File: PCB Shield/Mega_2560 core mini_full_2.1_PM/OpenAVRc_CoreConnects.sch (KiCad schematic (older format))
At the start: 18 parts, among them P1 2560-core, P10 RX1TX1, P16 LCD, P6 Micro_sd, P9 SPI, Q1 BSS84

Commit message: Update pcb files v2.1
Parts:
- added R10: 100, Resistors_SMD:R_1206, symbol R-RESCUE-Mega_2560_core_mini_full_2.0
- RV1: value 220K -> 10K
- RV6: value 22K -> 500
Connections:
- net at P16.18 (P18): now also R10.1; no longer RV6.2
- new net: R10.2, RV6.2
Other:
- moved on the sheet: RV6
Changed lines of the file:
@@
 Sheet 3 7
 Title "Shield Mega2560 core Full"
-Date "2018-01-30"
+Date "2018-01-31"
 Rev "2.10"
 Comp "© Team OpenAVRc"
@@
 $EndComp
 $Comp
-L GND-RESCUE-Mega_2560_core_mini_full_2.0 #PWR044
+L GND-RESCUE-Mega_2560_core_mini_full_2.0 #PWR51
 U 1 1 59C5DDBC
 P 4250 4450
-F 0 "#PWR044" H 4250 4200 50  0001 C CNN
+F 0 "#PWR51" H 4250 4200 50  0001 C CNN
 F 1 "GND" H 4250 4300 50  0000 C CNN
 F 2 "" H 4250 4450 50  0000 C CNN
@@
 $EndComp
 $Comp
-L VCC #PWR045
+L VCC #PWR49
 U 1 1 59C5DDC2
 P 3900 4700
-F 0 "#PWR045" H 3900 4550 50  0001 C CNN
+F 0 "#PWR49" H 3900 4550 50  0001 C CNN
 F 1 "VCC" V 3900 4900 50  0000 C CNN
 F 2 "" H 3900 4700 50  0000 C CNN
@@
 $EndComp
 $Comp
-L GND-RESCUE-Mega_2560_core_mini_full_2.0 #PWR046
+L GND-RESCUE-Mega_2560_core_mini_full_2.0 #PWR47
 U 1 1 59C5DDC8
 P 3400 1700
-F 0 "#PWR046" H 3400 1450 50  0001 C CNN
+F 0 "#PWR47" H 3400 1450 50  0001 C CNN
 F 1 "GND" H 3400 1550 50  0000 C CNN
 F 2 "" H 3400 1700 50  0000 C CNN
@@
 $EndComp
 $Comp
-L VCC #PWR047
+L VCC #PWR48
 U 1 1 59C5DDCE
 P 3700 1700
-F 0 "#PWR047" H 3700 1550 50  0001 C CNN
+F 0 "#PWR48" H 3700 1550 50  0001 C CNN
 F 1 "VCC" H 3700 1850 50  0000 C CNN
 F 2 "" H 3700 1700 50  0000 C CNN
@@
 Mosi
 $Comp
-L GND-RESCUE-Mega_2560_core_mini_full_2.0 #PWR048
+L GND-RESCUE-Mega_2560_core_mini_full_2.0 #PWR55
 U 1 1 59C5DDDC
 P 4900 2450
-F 0 "#PWR048" H 4900 2200 50  0001 C CNN
+F 0 "#PWR55" H 4900 2200 50  0001 C CNN
 F 1 "GND" V 4900 2250 50  0000 C CNN
 F 2 "" H 4900 2450 50  0000 C CNN
@@
 $EndComp
 $Comp
-L VCC #PWR049
+L VCC #PWR54
 U 1 1 59C5DDE2
 P 4900 2250
-F 0 "#PWR049" H 4900 2100 50  0001 C CNN
+F 0 "#PWR54" H 4900 2100 50  0001 C CNN
 F 1 "VCC" V 4900 2450 50  0000 C CNN
 F 2 "" H 4900 2250 50  0000 C CNN
@@
 $EndComp
 $Comp
-L VCC #PWR050
+L VCC #PWR46
 U 1 1 59C5DDE8
 P 2600 2100
-F 0 "#PWR050" H 2600 1950 50  0001 C CNN
+F 0 "#PWR46" H 2600 1950 50  0001 C CNN
 F 1 "VCC" V 2600 2300 50  0000 C CNN
 F 2 "" H 2600 2100 50  0000 C CNN
@@
 Lcd_bla
 $Comp
-L GND-RESCUE-Mega_2560_core_mini_full_2.0 #PWR051
+L GND-RESCUE-Mega_2560_core_mini_full_2.0 #PWR44
 U 1 1 59C5DE25
 P 1850 4450
-F 0 "#PWR051" H 1850 4200 50  0001 C CNN
+F 0 "#PWR44" H 1850 4200 50  0001 C CNN
 F 1 "GND" H 1850 4300 50  0000 C CNN
 F 2 "" H 1850 4450 50  0000 C CNN
@@
 $EndComp
 $Comp
-L GND-RESCUE-Mega_2560_core_mini_full_2.0 #PWR052
+L GND-RESCUE-Mega_2560_core_mini_full_2.0 #PWR45
 U 1 1 59C5DE2D
 P 2350 5300
-F 0 "#PWR052" H 2350 5050 50  0001 C CNN
+F 0 "#PWR45" H 2350 5050 50  0001 C CNN
 F 1 "GND" H 2350 5150 50  0000 C CNN
 F 2 "" H 2350 5300 50  0000 C CNN
@@
 $EndComp
 $Comp
-L GND-RESCUE-Mega_2560_core_mini_full_2.0 #PWR053
+L GND-RESCUE-Mega_2560_core_mini_full_2.0 #PWR52
 U 1 1 59C5DE45
 P 4550 4450
-F 0 "#PWR053" H 4550 4200 50  0001 C CNN
+F 0 "#PWR52" H 4550 4200 50  0001 C CNN
 F 1 "GND" H 4550 4300 50  0000 C CNN
 F 2 "" H 4550 4450 50  0000 C CNN
@@
 $EndComp
 $Comp
-L GND-RESCUE-Mega_2560_core_mini_full_2.0 #PWR054
+L GND-RESCUE-Mega_2560_core_mini_full_2.0 #PWR50
 U 1 1 59C5DE66
 P 4150 4950
-F 0 "#PWR054" H 4150 4700 50  0001 C CNN
+F 0 "#PWR50" H 4150 4700 50  0001 C CNN
 F 1 "GND" H 4150 4800 50  0000 C CNN
 F 2 "" H 4150 4950 50  0000 C CNN
@@
 $EndComp
 $Comp
-L GND-RESCUE-Mega_2560_core_mini_full_2.0 #PWR055
+L GND-RESCUE-Mega_2560_core_mini_full_2.0 #PWR43
 U 1 1 59C5DE7A
 P 1400 2100
-F 0 "#PWR055" H 1400 1850 50  0001 C CNN
+F 0 "#PWR43" H 1400 1850 50  0001 C CNN
 F 1 "GND" H 1400 1950 50  0000 C CNN
 F 2 "" H 1400 2100 50  0000 C CNN
@@
 $EndComp
 $Comp
-L GND-RESCUE-Mega_2560_core_mini_full_2.0 #PWR056
+L GND-RESCUE-Mega_2560_core_mini_full_2.0 #PWR53
 U 1 1 59C5DE80
 P 4850 2100
-F 0 "#PWR056" H 4850 1850 50  0001 C CNN
+F 0 "#PWR53" H 4850 1850 50  0001 C CNN
 F 1 "GND" V 4850 1900 50  0000 C CNN
 F 2 "" H 4850 2100 50  0000 C CNN
@@
 $EndComp
 $Comp
-L GND-RESCUE-Mega_2560_core_mini_full_2.0 #PWR057
+L GND-RESCUE-Mega_2560_core_mini_full_2.0 #PWR57
 U 1 1 59C5BE4B
 P 7050 2100
-F 0 "#PWR057" H 7050 1850 50  0001 C CNN
+F 0 "#PWR57" H 7050 1850 50  0001 C CNN
 F 1 "GND" H 7050 1950 50  0000 C CNN
 F 2 "" H 7050 2100 50  0000 C CNN
@@
 $EndComp
 $Comp
-L VCC #PWR058
+L VCC #PWR56
 U 1 1 59C5BE51
 P 6750 2100
-F 0 "#PWR058" H 6750 1950 50  0001 C CNN
+F 0 "#PWR56" H 6750 1950 50  0001 C CNN
 F 1 "VCC" H 6750 2250 50  0000 C CNN
 F 2 "" H 6750 2100 50  0000 C CNN
@@
 Miso
 $Comp
-L GND-RESCUE-Mega_2560_core_mini_full_2.0 #PWR059
+L GND-RESCUE-Mega_2560_core_mini_full_2.0 #PWR61
 U 1 1 59C5BE5B
 P 8750 1800
-F 0 "#PWR059" H 8750 1550 50  0001 C CNN
+F 0 "#PWR61" H 8750 1550 50  0001 C CNN
 F 1 "GND" H 8750 1650 50  0000 C CNN
 F 2 "" H 8750 1800 50  0000 C CNN
@@
 Text Label 10350 2050 1    60   ~ 0
 Lcd_rst
-Text Label 10200 2950 1    60   ~ 0
+Text Label 10200 3250 1    60   ~ 0
 Lcd_bla
 Text Label 10550 2050 1    60   ~ 0
@@
 Lcd_cs
 $Comp
-L GND-RESCUE-Mega_2560_core_mini_full_2.0 #PWR060
+L GND-RESCUE-Mega_2560_core_mini_full_2.0 #PWR64
 U 1 1 59C5BE7F
 P 10550 2050
-F 0 "#PWR060" H 10550 1800 50  0001 C CNN
+F 0 "#PWR64" H 10550 1800 50  0001 C CNN
 F 1 "GND" H 10550 1900 50  0000 C CNN
 F 2 "" H 10550 2050 50  0000 C CNN
@@
 Lcd_db5
 $Comp
-L GND-RESCUE-Mega_2560_core_mini_full_2.0 #PWR061
+L GND-RESCUE-Mega_2560_core_mini_full_2.0 #PWR62
 U 1 1 59C5BE86
 P 9150 2650
-F 0 "#PWR061" H 9150 2400 50  0001 C CNN
+F 0 "#PWR62" H 9150 2400 50  0001 C CNN
 F 1 "GND" H 9150 2500 50  0000 C CNN
 F 2 "" H 9150 2650 50  0000 C CNN
@@
 L POT-RESCUE-Mega_2560_core_mini_full_2.0 RV6
 U 1 1 59C5BE8C
-P 10200 2400
-F 0 "RV6" V 10025 2400 50  0000 C CNN
-F 1 "22K" V 10100 2400 50  0000 C CNN
-F 2 "Potentiometers:Potentiometer_Trimmer_Bourns_3296W" H 10200 2400 50  0001 C CNN
-F 3 "" H 10200 2400 50  0000 C CNN
-	1    10200 2400
+P 10200 2700
+F 0 "RV6" V 10100 2700 50  0000 C CNN
+F 1 "500" V 10200 2700 50  0000 C CNN
+F 2 "Potentiometers:Potentiometer_Trimmer_Bourns_3296W" H 10200 2700 50  0001 C CNN
+F 3 "" H 10200 2700 50  0000 C CNN
+	1    10200 2700
 	1    0    0    -1
 $EndComp
@@
 U 1 1 59C5BE93
 P 9150 2400
-F 0 "RV1" V 8975 2400 50  0000 C CNN
-F 1 "220K" V 9050 2400 50  0000 C CNN
+F 0 "RV1" V 9050 2400 50  0000 C CNN
+F 1 "10K" V 9150 2400 50  0000 C CNN
 F 2 "Potentiometers:Potentiometer_Trimmer_Bourns_3296W" H 9150 2400 50  0001 C CNN
 F 3 "" H 9150 2400 50  0000 C CNN
@@
 $EndComp
 $Comp
-L GND-RESCUE-Mega_2560_core_mini_full_2.0 #PWR062
+L GND-RESCUE-Mega_2560_core_mini_full_2.0 #PWR59
 U 1 1 59C5BEA8
 P 8100 4850
-F 0 "#PWR062" H 8100 4600 50  0001 C CNN
+F 0 "#PWR59" H 8100 4600 50  0001 C CNN
 F 1 "GND" H 8100 4700 50  0000 C CNN
 F 2 "" H 8100 4850 50  0000 C CNN
@@
 $EndComp
 $Comp
-L GND-RESCUE-Mega_2560_core_mini_full_2.0 #PWR063
+L GND-RESCUE-Mega_2560_core_mini_full_2.0 #PWR60
 U 1 1 59C5BEAE
 P 8500 5200
-F 0 "#PWR063" H 8500 4950 50  0001 C CNN
+F 0 "#PWR60" H 8500 4950 50  0001 C CNN
 F 1 "GND" H 8500 5050 50  0000 C CNN
 F 2 "" H 8500 5200 50  0000 C CNN
@@
 	8100 4600 8100 4850
 Wire Wire Line
-	10450 2400 10350 2400
-Wire Wire Line
 	9000 2250 9000 2400
 Wire Wire Line
@@
 	8950 1650 8950 2150
 Wire Wire Line
-	10450 1650 10450 2400
+	10450 1650 10450 2200
 Wire Wire Line
 	6750 1600 6750 2100
 Wire Wire Line
-	10200 2550 10200 2950
+	10200 2850 10200 3250
 Wire Wire Line
 	10350 1650 10350 2050
@@
 $EndComp
 $Comp
-L VCC #PWR064
+L VCC #PWR63
 U 1 1 59E0DFF9
 P 9600 4550
-F 0 "#PWR064" H 9600 4400 50  0001 C CNN
+F 0 "#PWR63" H 9600 4400 50  0001 C CNN
 F 1 "VCC" H 9600 4700 50  0000 C CNN
 F 2 "" H 9600 4550 50  0000 C CNN
@@
 $EndComp
 Wire Wire Line
-	7900 5500 7900 5000
+	7900 5000 7900 5500
 Wire Wire Line
 	7900 4700 7900 4600
@@
 	7500 5050 7400 5050
 $Comp
-L GND-RESCUE-Mega_2560_core_mini_full_2.0 #PWR065
+L GND-RESCUE-Mega_2560_core_mini_full_2.0 #PWR58
 U 1 1 59EF4C7A
 P 7400 5050
-F 0 "#PWR065" H 7400 4800 50  0001 C CNN
+F 0 "#PWR58" H 7400 4800 50  0001 C CNN
 F 1 "GND" H 7400 4900 50  0000 C CNN
 F 2 "" H 7400 5050 50  0000 C CNN
@@
 	0    1    1    0
 $EndComp
+$Comp
+L R-RESCUE-Mega_2560_core_mini_full_2.0 R10
+U 1 1 5A718CF7
+P 10450 2350
+F 0 "R10" V 10350 2350 50  0000 C CNN
+F 1 "100" V 10450 2350 50  0000 C CNN
+F 2 "Resistors_SMD:R_1206" V 10380 2350 50  0001 C CNN
+F 3 "" H 10450 2350 50  0000 C CNN
+	1    10450 2350
+	1    0    0    -1
+$EndComp
+Wire Wire Line
+	10450 2500 10450 2700
+Wire Wire Line
+	10450 2700 10350 2700
 $EndSCHEMATC

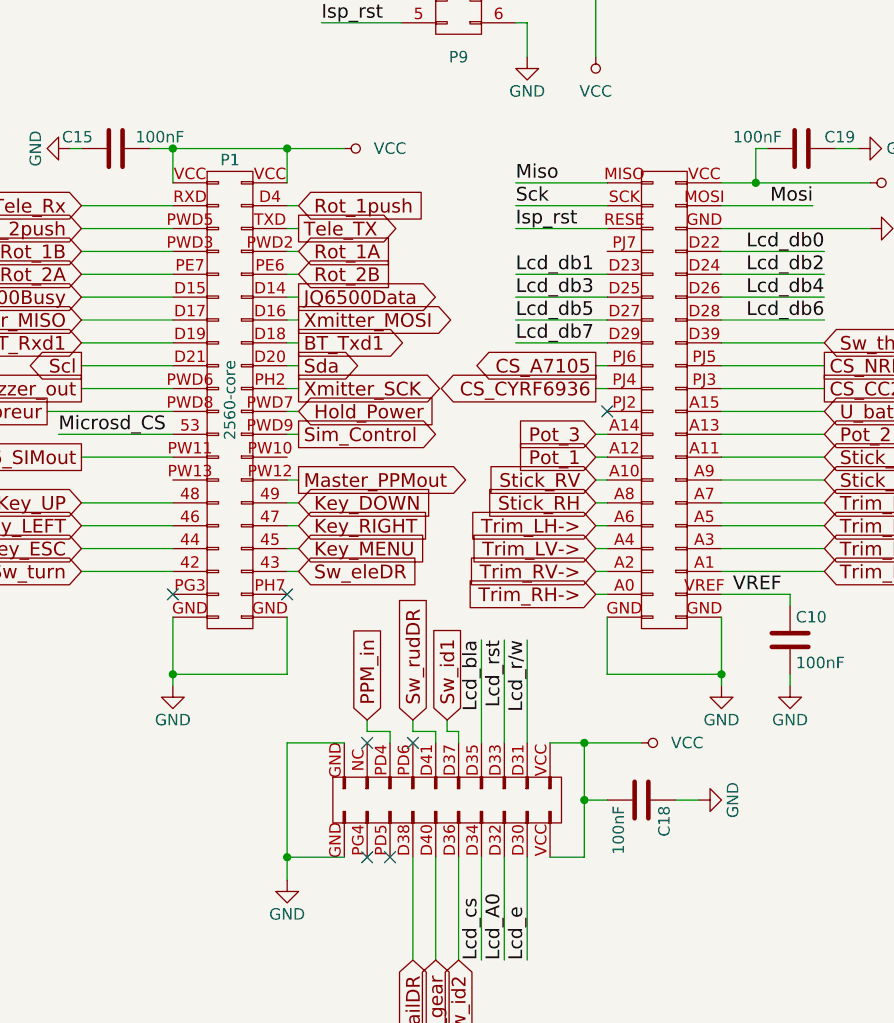
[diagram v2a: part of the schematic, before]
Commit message: Update pcb files v2.1
Add resistor 220 ohms on signal Tele_RX
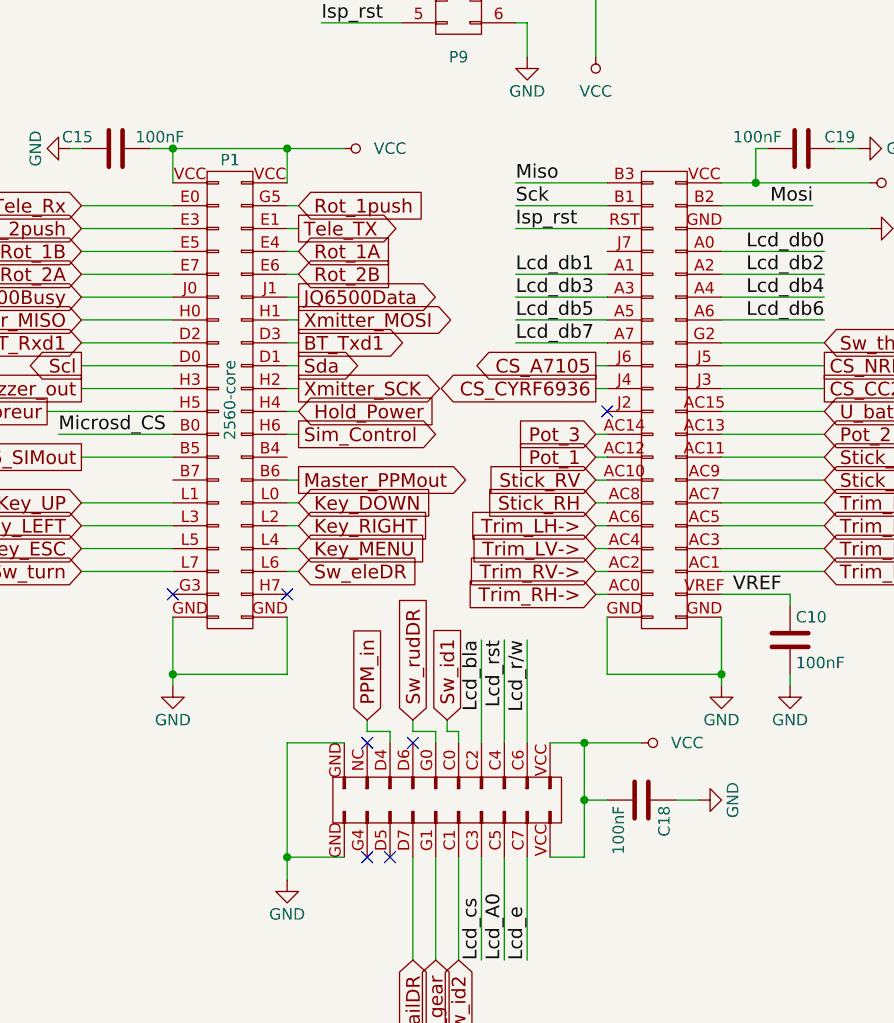
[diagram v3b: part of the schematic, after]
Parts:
- removed P1: 2560-core, anthoperso:Connectors-2560-core, symbol 2560-core
- added P1: 2560-core, symbol 2560-core-RESCUE-Mega_2560_core_mini_full_2.1
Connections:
- net Audio_Buzzer_out: now also P1.H3 (P20)
- net BT_Rxd1: now also P1.D2 (P16)
- net BT_Txd1: now also P1.D3 (P15)
- net CS_A7105: now also P1.J6 (P63)
- net CS_CC2500: now also P1.J3 (P62)
- net CS_CYRF6936: now also P1.J4 (P61)
- net CS_NRF24L01: now also P1.J5 (P64)
- net GND: now also P1.GND (P99)
- net Hold_Power: now also P1.H4 (P21)
- net Isp_rst: now also P1.RST (P75)
- net JQ6500Busy: now also P1.J0 (P12)
- net JQ6500Data: now also P1.J1 (P11)
- net Key_DOWN: now also P1.L0 (P29)
- net Key_ESC: now also P1.L5 (P34)
- net Key_LEFT: now also P1.L3 (P32)
- net Key_MENU: now also P1.L4 (P33)
- net Key_RIGHT: now also P1.L2 (P31)
- net Key_UP: now also P1.L1 (P30)
- net Lcd_A0: now also P1.C5 (P85)
- net Lcd_bla: now also P1.C2 (P88)
- net Lcd_cs: now also P1.C3 (P87)
- net Lcd_db0: now also P1.A0 (P74)
- net Lcd_db1: now also P1.A1 (P71)
- net Lcd_db2: now also P1.A2 (P72)
- net Lcd_db3: now also P1.A3 (P69)
- net Lcd_db4: now also P1.A4 (P70)
- net Lcd_db5: now also P1.A5 (P67)
- net Lcd_db6: now also P1.A6 (P68)
- net Lcd_db7: now also P1.A7 (P65)
- net Lcd_e: now also P1.C7 (P83)
- net Lcd_r/w: now also P1.C6 (P84)
- net Lcd_rst: now also P1.C4 (P86)
- net Master_PPMout: now also P1.B6 (P27)
- net Microsd_CS: now also P1.B0 (P24)
- net Miso: now also P1.B3 (P79)
- net Mosi: now also P1.B2 (P78)
- net PPM16_SIMout: now also P1.B5 (P26)
- net PPM_in: now also P1.D4 (P96)
- net Pot_1: now also P1.AC12 (P55)
- net Pot_2: now also P1.AC13 (P58)
- net Pot_3: now also P1.AC14 (P57)
- net Rot_1A: now also P1.E4 (P7)
- net Rot_1B: now also P1.E5 (P8)
- net Rot_1push: now also P1.G5 (P3)
- net Rot_2A: now also P1.E7 (P10)
- net Rot_2B: now also P1.E6 (P9)
- net Rot_2push: now also P1.E3 (P6)
- net Sck: now also P1.B1 (P77)
- net Scl: now also P1.D0 (P18)
- net Sda: now also P1.D1 (P17)
- net Sim_Control: now also P1.H6 (P23)
- net Stick_LH: now also P1.AC11 (P56)
- net Stick_LV: now also P1.AC9 (P54)
- net Stick_RH: now also P1.AC8 (P51)
- net Stick_RV: now also P1.AC10 (P53)
- net Sw_ailDR: now also P1.D7 (P93)
- net Sw_eleDR: now also P1.L6 (P35)
- net Sw_gear: now also P1.G1 (P91)
- net Sw_id1: now also P1.C0 (P90)
- net Sw_id2: now also P1.C1 (P89)
- net Sw_rudDR: now also P1.G0 (P92)
- net Sw_thcut: now also P1.G2 (P66)
- net Sw_turn: now also P1.L7 (P36)
- net Tele_Rx: now also P1.E0 (P4)
- net Tele_TX: now also P1.E1 (P5)
- net Trim_LH->: now also P1.AC6 (P49)
- net Trim_LH<-: now also P1.AC7 (P52)
- net Trim_LV->: now also P1.AC4 (P47)
- net Trim_LV<-: now also P1.AC5 (P50)
- net Trim_RH->: now also P1.AC0 (P43)
- net Trim_RH<-: now also P1.AC1 (P46)
- net Trim_RV->: now also P1.AC2 (P45)
- net Trim_RV<-: now also P1.AC3 (P48)
- net U_batt: now also P1.AC15 (P60)
- net VCC: now also P1.VCC (P82)
- net VREF: now also P1.VREF (P44)
- net Vibreur: now also P1.H5 (P22)
- net Xmitter_MISO: now also P1.H0 (P14)
- net Xmitter_MOSI: now also P1.H1 (P13)
- net Xmitter_SCK: now also P1.H2 (P19)
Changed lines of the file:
@@
 Sheet 3 7
 Title "Shield Mega2560 core Full"
-Date "2018-01-31"
+Date "2018-02-03"
 Rev "2.10"
 Comp "© Team OpenAVRc"
@@
 $EndComp
 $Comp
-L GND-RESCUE-Mega_2560_core_mini_full_2.0 #PWR045
+L GND-RESCUE-Mega_2560_core_mini_full_2.0 #PWR51
 U 1 1 59C5DDBC
 P 4250 4450
-F 0 "#PWR045" H 4250 4200 50  0001 C CNN
+F 0 "#PWR51" H 4250 4200 50  0001 C CNN
 F 1 "GND" H 4250 4300 50  0000 C CNN
 F 2 "" H 4250 4450 50  0000 C CNN
@@
 $EndComp
 $Comp
-L VCC #PWR046
+L VCC #PWR49
 U 1 1 59C5DDC2
 P 3900 4700
-F 0 "#PWR046" H 3900 4550 50  0001 C CNN
+F 0 "#PWR49" H 3900 4550 50  0001 C CNN
 F 1 "VCC" V 3900 4900 50  0000 C CNN
 F 2 "" H 3900 4700 50  0000 C CNN
@@
 $EndComp
 $Comp
-L GND-RESCUE-Mega_2560_core_mini_full_2.0 #PWR047
+L GND-RESCUE-Mega_2560_core_mini_full_2.0 #PWR47
 U 1 1 59C5DDC8
 P 3400 1700
-F 0 "#PWR047" H 3400 1450 50  0001 C CNN
+F 0 "#PWR47" H 3400 1450 50  0001 C CNN
 F 1 "GND" H 3400 1550 50  0000 C CNN
 F 2 "" H 3400 1700 50  0000 C CNN
@@
 $EndComp
 $Comp
-L VCC #PWR048
+L VCC #PWR48
 U 1 1 59C5DDCE
 P 3700 1700
-F 0 "#PWR048" H 3700 1550 50  0001 C CNN
+F 0 "#PWR48" H 3700 1550 50  0001 C CNN
 F 1 "VCC" H 3700 1850 50  0000 C CNN
 F 2 "" H 3700 1700 50  0000 C CNN
@@
 Mosi
 $Comp
-L GND-RESCUE-Mega_2560_core_mini_full_2.0 #PWR049
+L GND-RESCUE-Mega_2560_core_mini_full_2.0 #PWR55
 U 1 1 59C5DDDC
 P 4900 2450
-F 0 "#PWR049" H 4900 2200 50  0001 C CNN
+F 0 "#PWR55" H 4900 2200 50  0001 C CNN
 F 1 "GND" V 4900 2250 50  0000 C CNN
 F 2 "" H 4900 2450 50  0000 C CNN
@@
 $EndComp
 $Comp
-L VCC #PWR050
+L VCC #PWR54
 U 1 1 59C5DDE2
 P 4900 2250
-F 0 "#PWR050" H 4900 2100 50  0001 C CNN
+F 0 "#PWR54" H 4900 2100 50  0001 C CNN
 F 1 "VCC" V 4900 2450 50  0000 C CNN
 F 2 "" H 4900 2250 50  0000 C CNN
@@
 $EndComp
 $Comp
-L VCC #PWR051
+L VCC #PWR46
 U 1 1 59C5DDE8
 P 2600 2100
-F 0 "#PWR051" H 2600 1950 50  0001 C CNN
+F 0 "#PWR46" H 2600 1950 50  0001 C CNN
 F 1 "VCC" V 2600 2300 50  0000 C CNN
 F 2 "" H 2600 2100 50  0000 C CNN
@@
 Lcd_bla
 $Comp
-L GND-RESCUE-Mega_2560_core_mini_full_2.0 #PWR052
+L GND-RESCUE-Mega_2560_core_mini_full_2.0 #PWR44
 U 1 1 59C5DE25
 P 1850 4450
-F 0 "#PWR052" H 1850 4200 50  0001 C CNN
+F 0 "#PWR44" H 1850 4200 50  0001 C CNN
 F 1 "GND" H 1850 4300 50  0000 C CNN
 F 2 "" H 1850 4450 50  0000 C CNN
@@
 $EndComp
 $Comp
-L GND-RESCUE-Mega_2560_core_mini_full_2.0 #PWR053
+L GND-RESCUE-Mega_2560_core_mini_full_2.0 #PWR45
 U 1 1 59C5DE2D
 P 2350 5300
-F 0 "#PWR053" H 2350 5050 50  0001 C CNN
+F 0 "#PWR45" H 2350 5050 50  0001 C CNN
 F 1 "GND" H 2350 5150 50  0000 C CNN
 F 2 "" H 2350 5300 50  0000 C CNN
@@
 $EndComp
 $Comp
-L GND-RESCUE-Mega_2560_core_mini_full_2.0 #PWR054
+L GND-RESCUE-Mega_2560_core_mini_full_2.0 #PWR52
 U 1 1 59C5DE45
 P 4550 4450
-F 0 "#PWR054" H 4550 4200 50  0001 C CNN
+F 0 "#PWR52" H 4550 4200 50  0001 C CNN
 F 1 "GND" H 4550 4300 50  0000 C CNN
 F 2 "" H 4550 4450 50  0000 C CNN
@@
 $EndComp
 $Comp
-L GND-RESCUE-Mega_2560_core_mini_full_2.0 #PWR055
+L GND-RESCUE-Mega_2560_core_mini_full_2.0 #PWR50
 U 1 1 59C5DE66
 P 4150 4950
-F 0 "#PWR055" H 4150 4700 50  0001 C CNN
+F 0 "#PWR50" H 4150 4700 50  0001 C CNN
 F 1 "GND" H 4150 4800 50  0000 C CNN
 F 2 "" H 4150 4950 50  0000 C CNN
@@
 $EndComp
 $Comp
-L GND-RESCUE-Mega_2560_core_mini_full_2.0 #PWR056
+L GND-RESCUE-Mega_2560_core_mini_full_2.0 #PWR43
 U 1 1 59C5DE7A
 P 1400 2100
-F 0 "#PWR056" H 1400 1850 50  0001 C CNN
+F 0 "#PWR43" H 1400 1850 50  0001 C CNN
 F 1 "GND" H 1400 1950 50  0000 C CNN
 F 2 "" H 1400 2100 50  0000 C CNN
@@
 $EndComp
 $Comp
-L GND-RESCUE-Mega_2560_core_mini_full_2.0 #PWR057
+L GND-RESCUE-Mega_2560_core_mini_full_2.0 #PWR53
 U 1 1 59C5DE80
 P 4850 2100
-F 0 "#PWR057" H 4850 1850 50  0001 C CNN
+F 0 "#PWR53" H 4850 1850 50  0001 C CNN
 F 1 "GND" V 4850 1900 50  0000 C CNN
 F 2 "" H 4850 2100 50  0000 C CNN
@@
 	1    4850 2100
 	0    -1   -1   0
-$EndComp
-$Comp
-L 2560-core P1
-U 1 1 59C5DE8E
-P 50 3400
-F 0 "P1" H 2100 4650 50  0000 C CNN
-F 1 "2560-core" V 2100 3600 50  0000 C CNN
-F 2 "anthoperso:Connectors-2560-core" H 2100 2650 50  0001 C CNN
-F 3 "" H 2100 2650 50  0000 C CNN
-	1    50   3400
-	1    0    0    -1
 $EndComp
 $Comp
@@
 $EndComp
 $Comp
-L GND-RESCUE-Mega_2560_core_mini_full_2.0 #PWR058
+L GND-RESCUE-Mega_2560_core_mini_full_2.0 #PWR57
 U 1 1 59C5BE4B
 P 7050 2100
-F 0 "#PWR058" H 7050 1850 50  0001 C CNN
+F 0 "#PWR57" H 7050 1850 50  0001 C CNN
 F 1 "GND" H 7050 1950 50  0000 C CNN
 F 2 "" H 7050 2100 50  0000 C CNN
@@
 $EndComp
 $Comp
-L VCC #PWR059
+L VCC #PWR56
 U 1 1 59C5BE51
 P 6750 2100
-F 0 "#PWR059" H 6750 1950 50  0001 C CNN
+F 0 "#PWR56" H 6750 1950 50  0001 C CNN
 F 1 "VCC" H 6750 2250 50  0000 C CNN
 F 2 "" H 6750 2100 50  0000 C CNN
@@
 Miso
 $Comp
-L GND-RESCUE-Mega_2560_core_mini_full_2.0 #PWR060
+L GND-RESCUE-Mega_2560_core_mini_full_2.0 #PWR61
 U 1 1 59C5BE5B
 P 8750 1800
-F 0 "#PWR060" H 8750 1550 50  0001 C CNN
+F 0 "#PWR61" H 8750 1550 50  0001 C CNN
 F 1 "GND" H 8750 1650 50  0000 C CNN
 F 2 "" H 8750 1800 50  0000 C CNN
@@
 Lcd_cs
 $Comp
-L GND-RESCUE-Mega_2560_core_mini_full_2.0 #PWR061
+L GND-RESCUE-Mega_2560_core_mini_full_2.0 #PWR64
 U 1 1 59C5BE7F
 P 10550 2050
-F 0 "#PWR061" H 10550 1800 50  0001 C CNN
+F 0 "#PWR64" H 10550 1800 50  0001 C CNN
 F 1 "GND" H 10550 1900 50  0000 C CNN
 F 2 "" H 10550 2050 50  0000 C CNN
@@
 Lcd_db5
 $Comp
-L GND-RESCUE-Mega_2560_core_mini_full_2.0 #PWR062
+L GND-RESCUE-Mega_2560_core_mini_full_2.0 #PWR62
 U 1 1 59C5BE86
 P 9150 2650
-F 0 "#PWR062" H 9150 2400 50  0001 C CNN
+F 0 "#PWR62" H 9150 2400 50  0001 C CNN
 F 1 "GND" H 9150 2500 50  0000 C CNN
 F 2 "" H 9150 2650 50  0000 C CNN
@@
 $EndComp
 $Comp
-L GND-RESCUE-Mega_2560_core_mini_full_2.0 #PWR063
+L GND-RESCUE-Mega_2560_core_mini_full_2.0 #PWR59
 U 1 1 59C5BEA8
 P 8100 4850
-F 0 "#PWR063" H 8100 4600 50  0001 C CNN
+F 0 "#PWR59" H 8100 4600 50  0001 C CNN
 F 1 "GND" H 8100 4700 50  0000 C CNN
 F 2 "" H 8100 4850 50  0000 C CNN
@@
 $EndComp
 $Comp
-L GND-RESCUE-Mega_2560_core_mini_full_2.0 #PWR064
+L GND-RESCUE-Mega_2560_core_mini_full_2.0 #PWR60
 U 1 1 59C5BEAE
 P 8500 5200
-F 0 "#PWR064" H 8500 4950 50  0001 C CNN
+F 0 "#PWR60" H 8500 4950 50  0001 C CNN
 F 1 "GND" H 8500 5050 50  0000 C CNN
 F 2 "" H 8500 5200 50  0000 C CNN
@@
 $EndComp
 $Comp
-L VCC #PWR065
+L VCC #PWR63
 U 1 1 59E0DFF9
 P 9600 4550
-F 0 "#PWR065" H 9600 4400 50  0001 C CNN
+F 0 "#PWR63" H 9600 4400 50  0001 C CNN
 F 1 "VCC" H 9600 4700 50  0000 C CNN
 F 2 "" H 9600 4550 50  0000 C CNN
@@
 	7500 5050 7400 5050
 $Comp
-L GND-RESCUE-Mega_2560_core_mini_full_2.0 #PWR066
+L GND-RESCUE-Mega_2560_core_mini_full_2.0 #PWR58
 U 1 1 59EF4C7A
 P 7400 5050
-F 0 "#PWR066" H 7400 4800 50  0001 C CNN
+F 0 "#PWR58" H 7400 4800 50  0001 C CNN
 F 1 "GND" H 7400 4900 50  0000 C CNN
 F 2 "" H 7400 5050 50  0000 C CNN
@@
 Wire Wire Line
 	10450 2700 10350 2700
+$Comp
+L 2560-core-RESCUE-Mega_2560_core_mini_full_2.1 P1
+U 1 1 5A758C27
+P 50 3400
+AR Path="/5A758C27" Ref="P1"  Part="1"
+AR Path="/59C5D60D/5A758C27" Ref="P1"  Part="1"
+F 0 "P1" H 2100 4650 50  0000 C CNN
+F 1 "2560-core" V 2100 3600 50  0000 C CNN
+F 2 "" H 2100 2650 50  0000 C CNN
+F 3 "" H 2100 2650 50  0000 C CNN
+	1    50   3400
+	1    0    0    -1
+$EndComp
 $EndSCHEMATC
